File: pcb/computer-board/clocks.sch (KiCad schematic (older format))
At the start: 11 parts, among them J5 Conn_01x04_Male, J6 Conn_01x02, U16 DS1077LZ-60+, U17 74LVC1G157GC-Q100H, U18 74LVC1G14GW,125

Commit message: Remove and change connectors for a mezzanine one
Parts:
- removed J5: Conn_01x04_Male, Connector_Molex:Molex_Pico-Clasp_202396-0407_1x04-1MP_P1.00mm_Horizontal, symbol Connector:Conn_01x04_Male
- removed J6: Conn_01x02, Connector_Molex:Molex_Pico-Clasp_202396-0207_1x02-1MP_P1.00mm_Horizontal, symbol Connector_Generic:Conn_01x02
- added R? (x2): 10k, Resistor_SMD:R_0402_1005Metric_Pad0.72x0.64mm_HandSolder, symbol Device:R_Small
- added TP10, TP8: TestPoint_Small, TestPoint:TestPoint_THTPad_D1.5mm_Drill0.7mm, symbol Connector:TestPoint_Small
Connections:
- net +3V3: now also R?.1, R?.1
- net SCL: now also R?.2, TP8.1
- net SDA: now also R?.2, TP10.1
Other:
- note removed: "External clock connector"
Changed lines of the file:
@@
 Text Notes 650  2200 0    50   Italic 0
 CTRL0 and CTRL1 are tied\nto GND because we don’t \ncare about the power-down feature
-$Comp
-L Connector:Conn_01x04_Male J5
-U 1 1 5F90DBBD
-P 3300 1400
-F 0 "J5" H 3272 1282 50  0000 R CNN
-F 1 "Conn_01x04_Male" H 3650 1050 50  0000 R CNN
-F 2 "Connector_Molex:Molex_Pico-Clasp_202396-0407_1x04-1MP_P1.00mm_Horizontal" H 3300 1400 50  0001 C CNN
-F 3 "~" H 3300 1400 50  0001 C CNN
-	1    3300 1400
-	-1   0    0    1
-$EndComp
-Text GLabel 3100 1200 0    50   Output ~ 0
+Text GLabel 3050 1500 0    50   Output ~ 0
 SCL
-Text GLabel 3100 1400 0    50   BiDi ~ 0
+Text GLabel 3050 1600 0    50   BiDi ~ 0
 SDA
-$Comp
-L power:+3.3V #PWR0115
-U 1 1 5F90E1E6
-P 2800 1150
-F 0 "#PWR0115" H 2800 1000 50  0001 C CNN
-F 1 "+3.3V" H 2815 1323 50  0000 C CNN
-F 2 "" H 2800 1150 50  0001 C CNN
-F 3 "" H 2800 1150 50  0001 C CNN
-	1    2800 1150
-	1    0    0    -1
-$EndComp
-$Comp
-L power:GND #PWR0116
-U 1 1 5F90E750
-P 2800 1500
-F 0 "#PWR0116" H 2800 1250 50  0001 C CNN
-F 1 "GND" H 2805 1327 50  0000 C CNN
-F 2 "" H 2800 1500 50  0001 C CNN
-F 3 "" H 2800 1500 50  0001 C CNN
-	1    2800 1500
-	1    0    0    -1
-$EndComp
-Wire Wire Line
-	3100 1500 2800 1500
-Wire Wire Line
-	3100 1300 2800 1300
-Wire Wire Line
-	2800 1300 2800 1150
 Wire Notes Line
 	2650 850  3650 850
@@
 Text Notes 650  2650 0    50   ~ 0
 External clock selection
-Text GLabel 3150 3150 0    50   Output ~ 0
-EXT_CLK
-$Comp
-L power:GND #PWR0156
-U 1 1 5FAC1E07
-P 3200 3300
-F 0 "#PWR0156" H 3200 3050 50  0001 C CNN
-F 1 "GND" H 3205 3127 50  0000 C CNN
-F 2 "" H 3200 3300 50  0001 C CNN
-F 3 "" H 3200 3300 50  0001 C CNN
-	1    3200 3300
-	1    0    0    -1
-$EndComp
-Wire Wire Line
-	3150 3150 3250 3150
-Wire Notes Line
-	2650 2750 3600 2750
-Text Notes 2650 2750 0    50   ~ 0
-External clock connector
 $Comp
 L 74LVC1G157:74LVC1G157GC-Q100H U17
@@
 Text Notes 3850 1850 0    50   ~ 0
 Clock selection
-$Comp
-L Connector_Generic:Conn_01x02 J6
-U 1 1 5FAD3D98
-P 3450 3150
-F 0 "J6" H 3250 3400 50  0000 L CNN
-F 1 "Conn_01x02" H 3000 3300 50  0000 L CNN
-F 2 "Connector_Molex:Molex_Pico-Clasp_202396-0207_1x02-1MP_P1.00mm_Horizontal" H 3450 3150 50  0001 C CNN
-F 3 "~" H 3450 3150 50  0001 C CNN
-	1    3450 3150
-	1    0    0    -1
-$EndComp
-Wire Wire Line
-	3200 3250 3250 3250
-Wire Wire Line
-	3200 3300 3200 3250
-Wire Notes Line
-	2650 2750 2650 3550
-Wire Notes Line
-	2650 3550 3600 3550
-Wire Notes Line
-	3600 3550 3600 2750
 Text Notes 3850 2850 0    50   Italic 0
 The clock inversion happens locally
@@
 Wire Wire Line
 	850  3200 1150 3200
+$Comp
+L Connector:TestPoint_Small TP8
+U 1 1 605E9ACF
+P 3300 1500
+F 0 "TP8" H 3348 1500 50  0000 L CNN
+F 1 "TestPoint_Small" H 3348 1455 50  0001 L CNN
+F 2 "TestPoint:TestPoint_THTPad_D1.5mm_Drill0.7mm" H 3500 1500 50  0001 C CNN
+F 3 "~" H 3500 1500 50  0001 C CNN
+	1    3300 1500
+	1    0    0    -1
+$EndComp
+$Comp
+L Connector:TestPoint_Small TP10
+U 1 1 605EA570
+P 3300 1600
+F 0 "TP10" H 3348 1600 50  0000 L CNN
+F 1 "TestPoint_Small" H 3348 1555 50  0001 L CNN
+F 2 "TestPoint:TestPoint_THTPad_D1.5mm_Drill0.7mm" H 3500 1600 50  0001 C CNN
+F 3 "~" H 3500 1600 50  0001 C CNN
+	1    3300 1600
+	1    0    0    -1
+$EndComp
+$Comp
+L Device:R_Small R?
+U 1 1 60611F1F
+P 3100 1300
+F 0 "R?" H 2750 1350 50  0000 L CNN
+F 1 "10k" H 2750 1250 50  0000 L CNN
+F 2 "Resistor_SMD:R_0402_1005Metric_Pad0.72x0.64mm_HandSolder" H 3100 1300 50  0001 C CNN
+F 3 "~" H 3100 1300 50  0001 C CNN
+	1    3100 1300
+	1    0    0    -1
+$EndComp
+$Comp
+L Device:R_Small R?
+U 1 1 6061315C
+P 3200 1300
+F 0 "R?" H 2850 1350 50  0000 L CNN
+F 1 "10k" H 2900 1250 50  0000 L CNN
+F 2 "Resistor_SMD:R_0402_1005Metric_Pad0.72x0.64mm_HandSolder" H 3200 1300 50  0001 C CNN
+F 3 "~" H 3200 1300 50  0001 C CNN
+	1    3200 1300
+	1    0    0    -1
+$EndComp
+Wire Wire Line
+	3050 1500 3100 1500
+Wire Wire Line
+	3050 1600 3200 1600
+Wire Wire Line
+	3100 1400 3100 1500
+Connection ~ 3100 1500
+Wire Wire Line
+	3100 1500 3300 1500
+Wire Wire Line
+	3200 1400 3200 1600
+Connection ~ 3200 1600
+Wire Wire Line
+	3200 1600 3300 1600
+$Comp
+L power:+3.3V #PWR?
+U 1 1 6061491D
+P 3100 1200
+F 0 "#PWR?" H 3100 1050 50  0001 C CNN
+F 1 "+3.3V" H 2950 1350 50  0000 C CNN
+F 2 "" H 3100 1200 50  0001 C CNN
+F 3 "" H 3100 1200 50  0001 C CNN
+	1    3100 1200
+	1    0    0    -1
+$EndComp
+$Comp
+L power:+3.3V #PWR?
+U 1 1 60614E25
+P 3200 1200
+F 0 "#PWR?" H 3200 1050 50  0001 C CNN
+F 1 "+3.3V" H 3350 1350 50  0000 C CNN
+F 2 "" H 3200 1200 50  0001 C CNN
+F 3 "" H 3200 1200 50  0001 C CNN
+	1    3200 1200
+	1    0    0    -1
+$EndComp
 $EndSCHEMATC

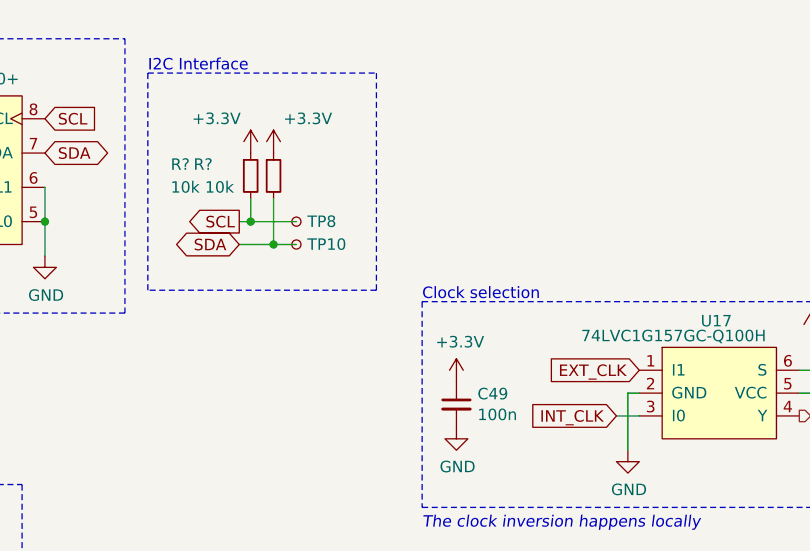
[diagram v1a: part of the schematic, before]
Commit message: Revision 2 is ready
Need to wait for the testing of rev 1 before ordering
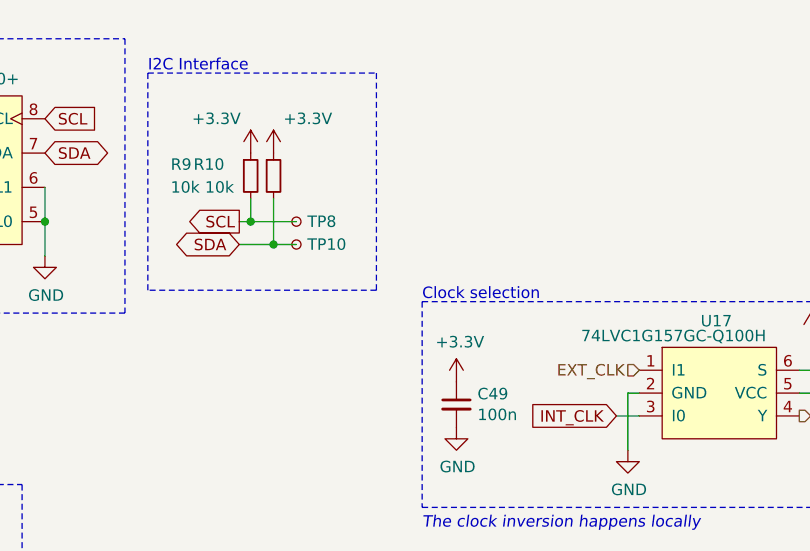
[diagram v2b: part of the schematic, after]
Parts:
- TP10, TP8: footprint TestPoint:TestPoint_THTPad_D1.5mm_Drill0.7mm -> TestPoint:TestPoint_THTPad_1.5x1.5mm_Drill0.7mm
- gave numbers to parts that had none: 2
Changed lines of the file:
@@
 	1    0    0    -1
 $EndComp
-Text GLabel 4800 2150 0    50   Input ~ 0
-EXT_CLK
 Text GLabel 4700 2350 0    50   Input ~ 0
 INT_CLK
@@
 F 0 "TP8" H 3348 1500 50  0000 L CNN
 F 1 "TestPoint_Small" H 3348 1455 50  0001 L CNN
-F 2 "TestPoint:TestPoint_THTPad_D1.5mm_Drill0.7mm" H 3500 1500 50  0001 C CNN
+F 2 "TestPoint:TestPoint_THTPad_1.5x1.5mm_Drill0.7mm" H 3500 1500 50  0001 C CNN
 F 3 "~" H 3500 1500 50  0001 C CNN
 	1    3300 1500
@@
 F 0 "TP10" H 3348 1600 50  0000 L CNN
 F 1 "TestPoint_Small" H 3348 1555 50  0001 L CNN
-F 2 "TestPoint:TestPoint_THTPad_D1.5mm_Drill0.7mm" H 3500 1600 50  0001 C CNN
+F 2 "TestPoint:TestPoint_THTPad_1.5x1.5mm_Drill0.7mm" H 3500 1600 50  0001 C CNN
 F 3 "~" H 3500 1600 50  0001 C CNN
 	1    3300 1600
@@
 $EndComp
 $Comp
-L Device:R_Small R?
+L Device:R_Small R9
 U 1 1 60611F1F
 P 3100 1300
-F 0 "R?" H 2750 1350 50  0000 L CNN
+F 0 "R9" H 2750 1350 50  0000 L CNN
 F 1 "10k" H 2750 1250 50  0000 L CNN
 F 2 "Resistor_SMD:R_0402_1005Metric_Pad0.72x0.64mm_HandSolder" H 3100 1300 50  0001 C CNN
@@
 $EndComp
 $Comp
-L Device:R_Small R?
+L Device:R_Small R10
 U 1 1 6061315C
 P 3200 1300
-F 0 "R?" H 2850 1350 50  0000 L CNN
+F 0 "R10" H 2850 1350 50  0000 L CNN
 F 1 "10k" H 2900 1250 50  0000 L CNN
 F 2 "Resistor_SMD:R_0402_1005Metric_Pad0.72x0.64mm_HandSolder" H 3200 1300 50  0001 C CNN
@@
 	3200 1600 3300 1600
 $Comp
-L power:+3.3V #PWR?
+L power:+3.3V #PWR0115
 U 1 1 6061491D
 P 3100 1200
-F 0 "#PWR?" H 3100 1050 50  0001 C CNN
+F 0 "#PWR0115" H 3100 1050 50  0001 C CNN
 F 1 "+3.3V" H 2950 1350 50  0000 C CNN
 F 2 "" H 3100 1200 50  0001 C CNN
@@
 $EndComp
 $Comp
-L power:+3.3V #PWR?
+L power:+3.3V #PWR0116
 U 1 1 60614E25
 P 3200 1200
-F 0 "#PWR?" H 3200 1050 50  0001 C CNN
+F 0 "#PWR0116" H 3200 1050 50  0001 C CNN
 F 1 "+3.3V" H 3350 1350 50  0000 C CNN
 F 2 "" H 3200 1200 50  0001 C CNN
@@
 	1    0    0    -1
 $EndComp
+Text HLabel 4800 2150 0    50   Input ~ 0
+EXT_CLK
 $EndSCHEMATC
